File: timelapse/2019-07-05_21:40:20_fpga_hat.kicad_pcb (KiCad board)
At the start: 4 copper layers, 65 x 56.5 mm, 91 parts, among them J1 2x20, J2 AudioJack3, J3 Conn_02x06_Top_Bottom, J4 Conn_02x06_Top_Bottom, J5 Conn_02x06_Top_Bottom, J6 Conn_01x02, SW1 PTS815, SW2 PTS815, SW3 PTS815, SW4 PTS815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

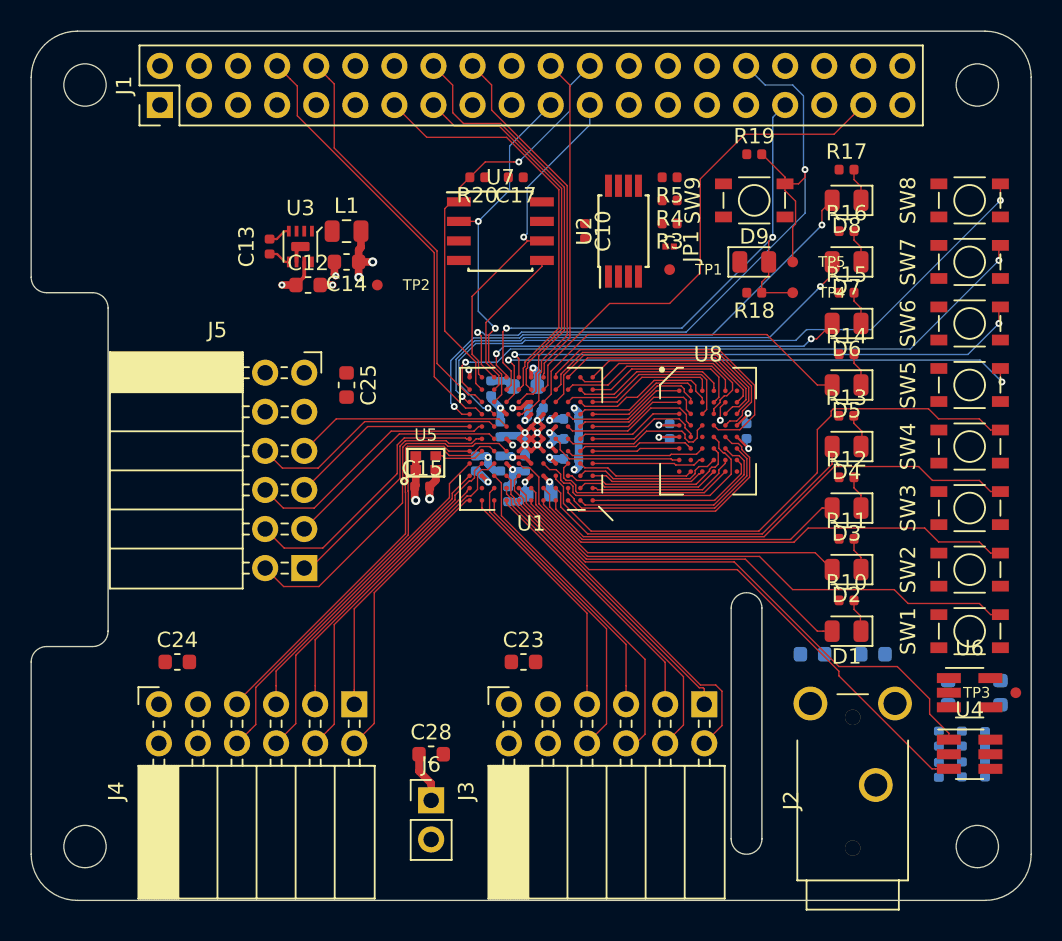
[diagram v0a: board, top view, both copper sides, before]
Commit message: Connect up SDIO, remaining buttons + LEDs.
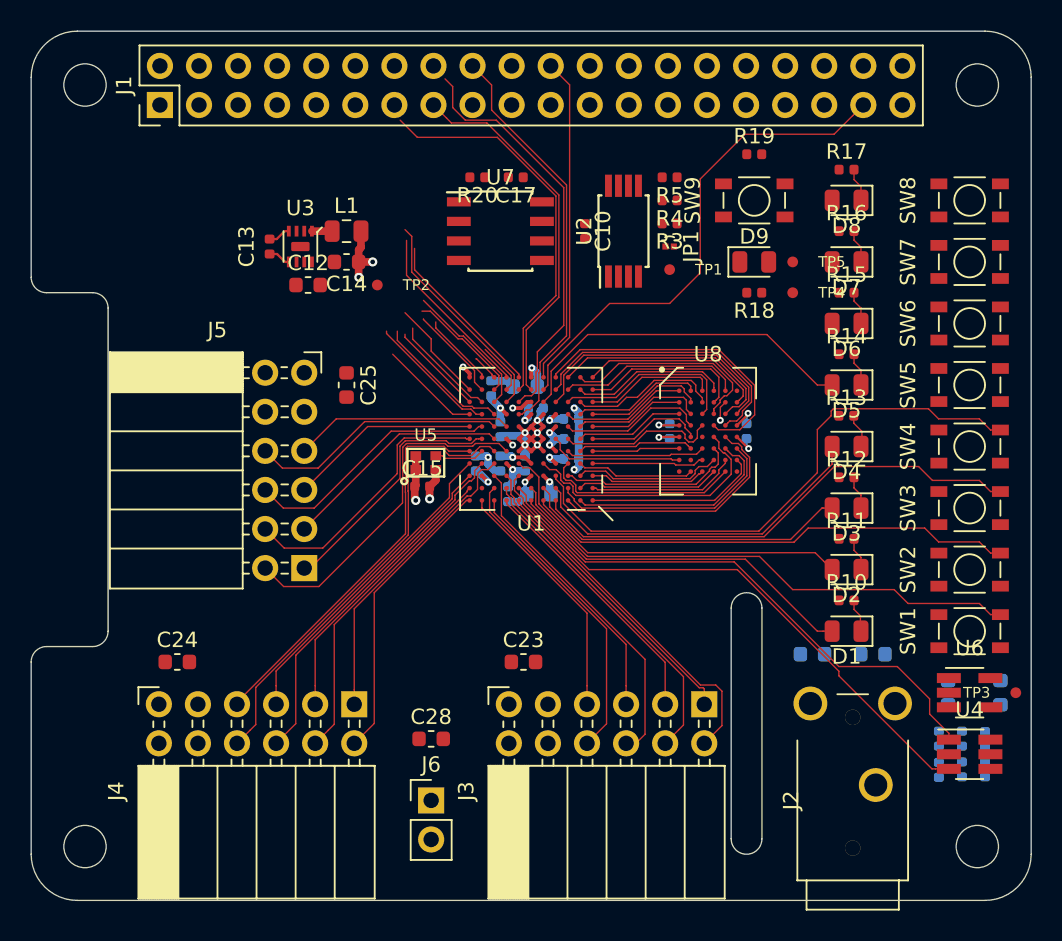
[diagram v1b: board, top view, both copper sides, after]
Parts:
- moved C28 1.00 mm to (126.0, 126.0)
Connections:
- U1 pad J7: /GP23_SDIO_CMD -> /SW4
- U1 pad J8: /SW4 -> /GP23_SDIO_CMD
- U1 pad K7: /GP27_SDIO_DAT3 -> /LED5
- U1 pad L8: /LED5 -> /GP27_SDIO_DAT3
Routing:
- net /GP12_FPGA_~RST: track 50.2 -> 1.73 mm, vias 2 -> 0
- net /SW4: track 36.7 -> 0.00 mm, vias 2 -> 0
- net /SW7: track 45.2 -> 8.89 mm, vias 2 -> 0
- net /GP13_FPGA_CDONE: track 39.0 -> 3.43 mm, vias 2 -> 0
- net /SW6: track 40.5 -> 6.74 mm, vias 2 -> 0
- net /LED7: track 33.9 -> 6.62 mm, vias 2 -> 0
- net /GP26_SDIO_DAT2: track 32.8 -> 59.6 mm
- net /LED6: track 30.8 -> 6.14 mm, vias 2 -> 0
- net /SW5: track 35.0 -> 11.2 mm, vias 2 -> 0
- net /GP8_SPI_~CS: track 27.5 -> 6.17 mm, vias 1 -> 0
- net /GP14_UART_TXD: track 28.5 -> 8.53 mm
- net /GP15_UART_RXD: track 26.5 -> 6.91 mm
- net /GP11_SPI_SCK: track 22.3 -> 4.84 mm, vias 1 -> 0
- net /GP27_SDIO_DAT3: track 27.5 -> 12.0 mm
- net /GP9_SPI_MISO: track 23.7 -> 9.06 mm, vias 2 -> 0
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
